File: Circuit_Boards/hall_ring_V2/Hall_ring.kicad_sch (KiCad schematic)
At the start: 18 parts, among them J1 T1M-06-X-DV, U1 DRV5053_LPG, U2 DRV5053_LPG, U3 DRV5053_LPG, U4 DRV5053_LPG, U5 DRV5053_LPG, U6 DRV5053_LPG, U7 DRV5053_LPG

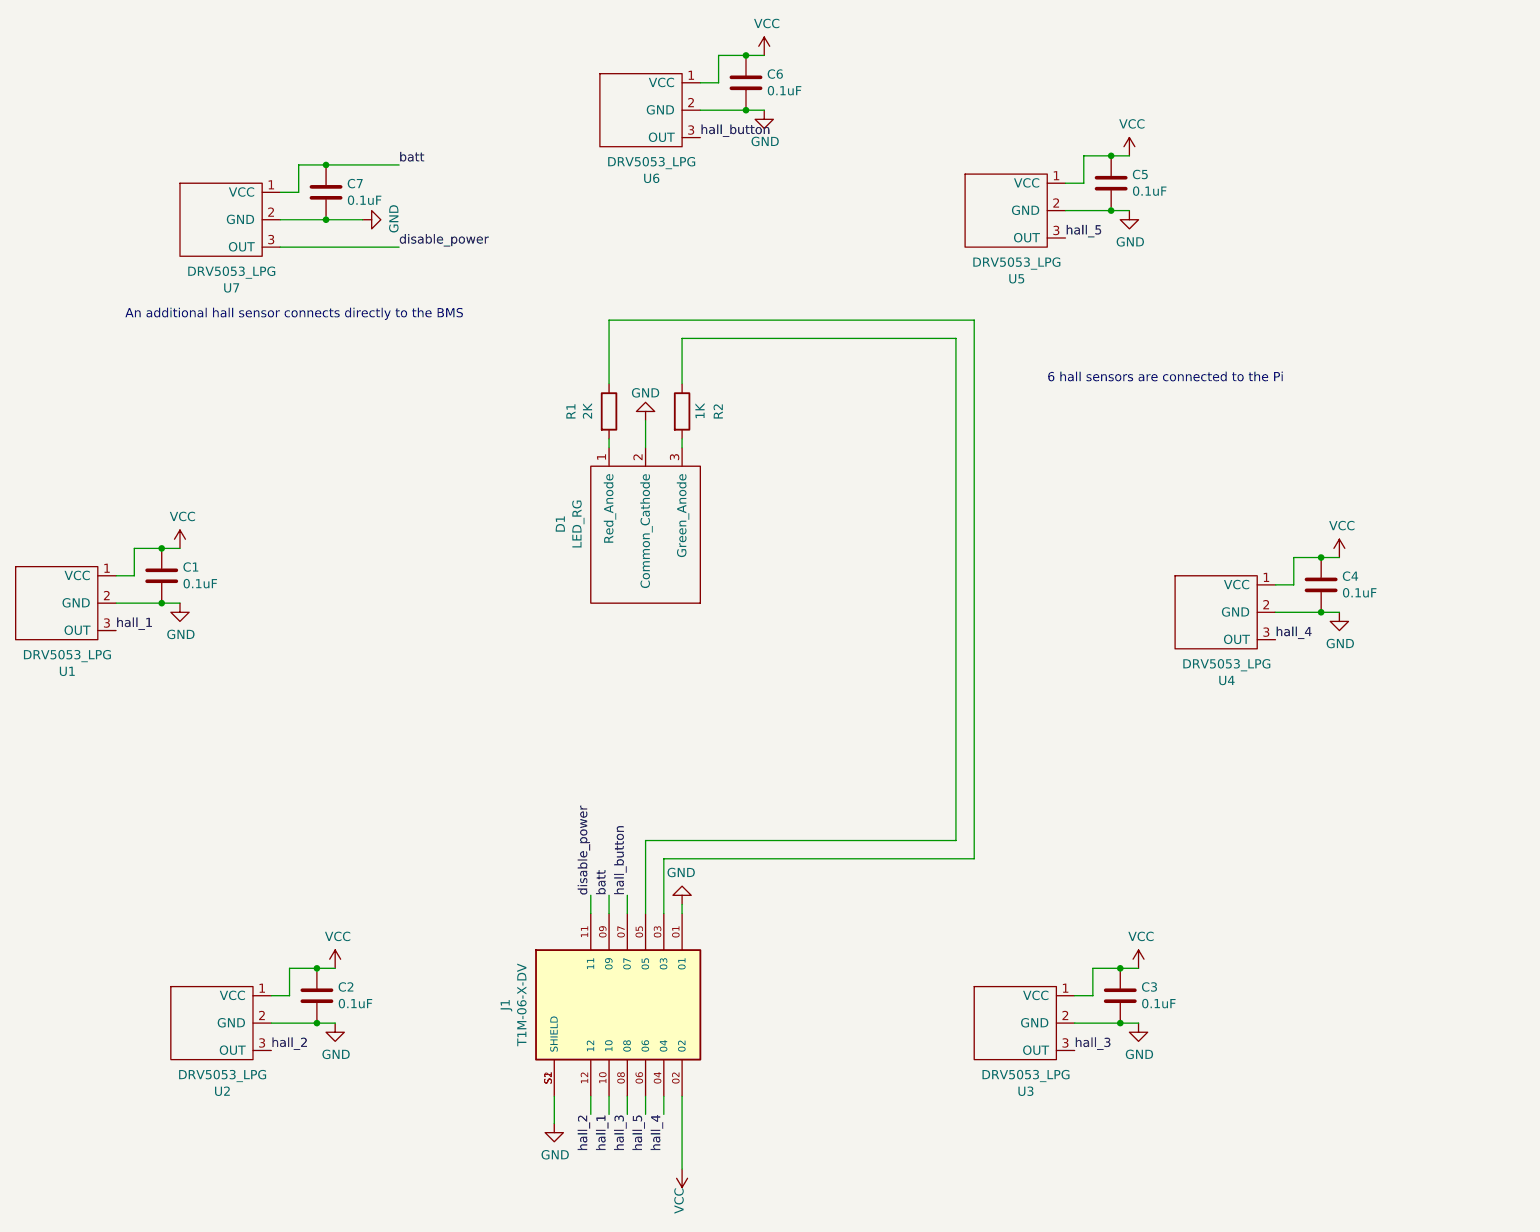
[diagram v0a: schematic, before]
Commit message: removed BOM and gerbers for kicad project, to ensure up to date exports
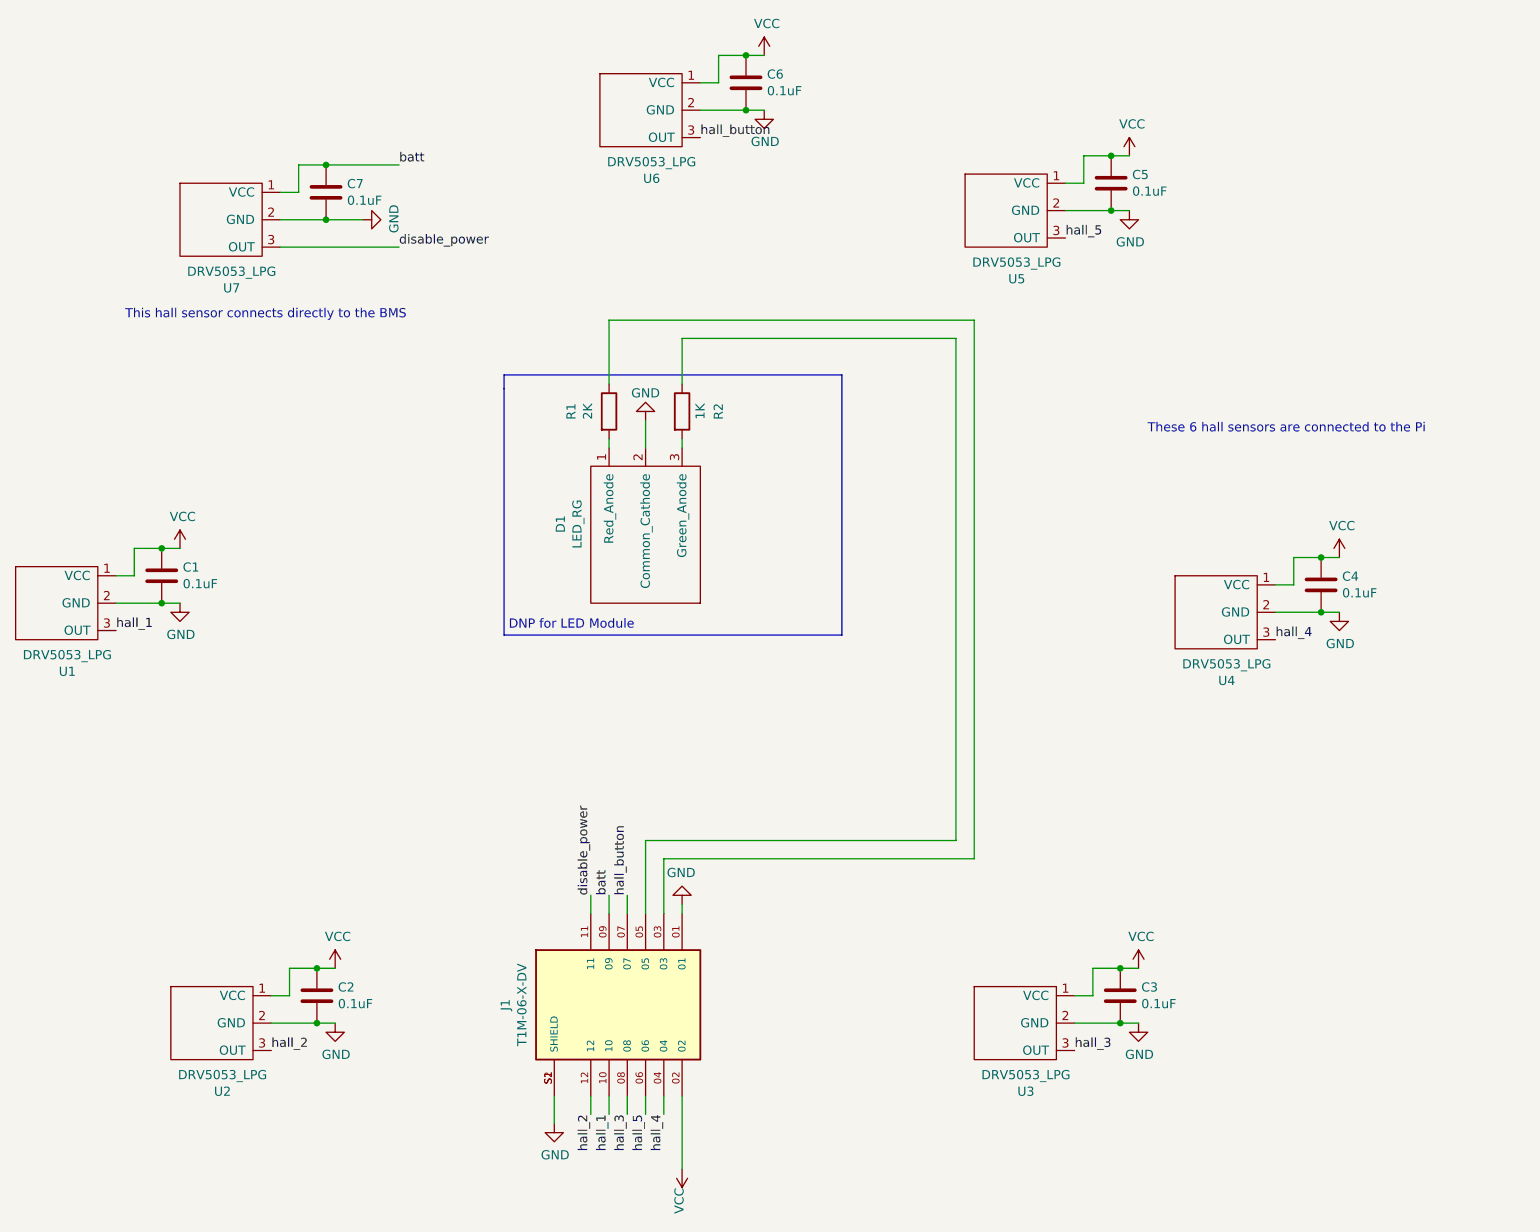
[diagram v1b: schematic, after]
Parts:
- C1, C2, C3, C4, C5, C6, C7, D1, J1, R1, R2, U1, U2, U3, U4, U5, U6, U7: Buy Digikey buy -> (none)
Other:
- note added: "DNP for LED Module"
- note added: "These 6 hall sensors are connected to the Pi"
- note added: "This hall sensor connects directly to the BMS"
- note removed: "6 hall sensors are connected to the Pi"
- note removed: "An additional hall sensor connects directly to the BMS"
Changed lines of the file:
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@@
+    (stroke (width 0) (type default) (color 0 0 0 0))
+  )
+  (polyline (pts (xy 165.735 63.5) (xy 118.745 63.5))
     (stroke (width 0) (type default) (color 0 0 0 0))
   )
@@
     (stroke (width 0) (type default) (color 0 0 0 0))
   )
+  (polyline (pts (xy 118.745 99.695) (xy 165.735 99.695))
+    (stroke (width 0) (type default) (color 0 0 0 0))
+  )
   (wire (pts (xy 92.71 146.05) (xy 95.25 146.05))
     (stroke (width 0) (type default) (color 0 0 0 0))
@@
     (stroke (width 0) (type default) (color 0 0 0 0))
   )
+  (polyline (pts (xy 118.745 65.405) (xy 118.745 99.695))
+    (stroke (width 0) (type default) (color 0 0 0 0))
+  )
   (wire (pts (xy 146.05 22.86) (xy 148.59 22.86))
     (stroke (width 0) (type default) (color 0 0 0 0))
@@
     (stroke (width 0) (type default) (color 0 0 0 0))
   )
+  (polyline (pts (xy 118.745 63.5) (xy 118.745 65.405))
+    (stroke (width 0) (type default) (color 0 0 0 0))
+  )
   (wire (pts (xy 181.61 128.27) (xy 181.61 58.42))
     (stroke (width 0) (type default) (color 0 0 0 0))
@@
     (stroke (width 0) (type default) (color 0 0 0 0))
   )
+  (polyline (pts (xy 165.735 99.695) (xy 165.735 63.5))
+    (stroke (width 0) (type default) (color 0 0 0 0))
+  )
   (wire (pts (xy 200.66 149.86) (xy 200.66 146.05))
     (stroke (width 0) (type default) (color 0 0 0 0))
@@
     (stroke (width 0) (type default) (color 0 0 0 0))
   )
-  (text "6 hall sensors are connected to the Pi\n" (at 194.31 64.77 0)
-    (effects (font (size 1.27 1.27)) (justify left bottom))
-  )
-  (text "An additional hall sensor connects directly to the BMS\n"
-    (at 66.04 55.88 0)
+  (text "DNP for LED Module" (at 119.38 99.06 0)
+    (effects (font (size 1.27 1.27)) (justify left bottom))
+  )
+  (text "These 6 hall sensors are connected to the Pi\n" (at 208.28 71.755 0)
+    (effects (font (size 1.27 1.27)) (justify left bottom))
+  )
+  (text "This hall sensor connects directly to the BMS\n" (at 66.04 55.88 0)
     (effects (font (size 1.27 1.27)) (justify left bottom))
   )
@@
       (effects (font (size 1.27 1.27)) hide)
     )
-    (property "Buy Digikey" "buy" (id 5) (at 57.15 101.6 0)
+    (property "Buy Digikey" "" (id 5) (at 57.15 101.6 0)
       (effects (font (size 1.27 1.27)) hide)
     )
@@
       (effects (font (size 1.27 1.27)) hide)
     )
-    (property "Buy Digikey" "buy" (id 5) (at 190.5 160.02 0)
+    (property "Buy Digikey" "" (id 5) (at 190.5 160.02 0)
       (effects (font (size 1.27 1.27)) hide)
     )
@@
       (effects (font (size 1.27 1.27)) hide)
     )
-    (property "Buy Digikey" "buy" (id 5) (at 218.44 102.87 0)
+    (property "Buy Digikey" "" (id 5) (at 218.44 102.87 0)
       (effects (font (size 1.27 1.27)) hide)
     )
@@
       (effects (font (size 1.27 1.27)) hide)
     )
-    (property "Buy Digikey" "buy" (id 5) (at 189.23 46.99 0)
+    (property "Buy Digikey" "" (id 5) (at 189.23 46.99 0)
       (effects (font (size 1.27 1.27)) hide)
     )
@@
       (effects (font (size 1.27 1.27)) hide)
     )
-    (property "Buy Digikey" "buy" (id 5) (at 138.43 33.02 0)
+    (property "Buy Digikey" "" (id 5) (at 138.43 33.02 0)
       (effects (font (size 1.27 1.27)) hide)
     )
@@
       (effects (font (size 1.27 1.27)) hide)
     )
-    (property "Buy Digikey" "buy" (id 5) (at 78.74 160.02 0)
+    (property "Buy Digikey" "" (id 5) (at 78.74 160.02 0)
       (effects (font (size 1.27 1.27)) hide)
     )
@@
       (effects (font (size 1.27 1.27)) hide)
     )
-    (property "Buy Digikey" "buy" (id 6) (at 71.12 91.44 0)
+    (property "Buy Digikey" "" (id 6) (at 71.12 91.44 0)
       (effects (font (size 1.27 1.27)) hide)
     )
@@
       (effects (font (size 1.27 1.27)) hide)
     )
-    (property "Buy Digikey" "buy" (id 6) (at 92.71 149.86 0)
+    (property "Buy Digikey" "" (id 6) (at 92.71 149.86 0)
       (effects (font (size 1.27 1.27)) hide)
     )
@@
       (effects (font (size 1.27 1.27)) hide)
     )
-    (property "Buy Digikey" "buy" (id 6) (at 204.47 149.86 0)
+    (property "Buy Digikey" "" (id 6) (at 204.47 149.86 0)
       (effects (font (size 1.27 1.27)) hide)
     )
@@
       (effects (font (size 1.27 1.27)) hide)
     )
-    (property "Buy Digikey" "buy" (id 6) (at 232.41 92.71 0)
+    (property "Buy Digikey" "" (id 6) (at 232.41 92.71 0)
       (effects (font (size 1.27 1.27)) hide)
     )
@@
       (effects (font (size 1.27 1.27)) hide)
     )
-    (property "Buy Digikey" "buy" (id 6) (at 203.2 36.83 0)
+    (property "Buy Digikey" "" (id 6) (at 203.2 36.83 0)
       (effects (font (size 1.27 1.27)) hide)
     )
@@
       (effects (font (size 1.27 1.27)) hide)
     )
-    (property "Buy Digikey" "buy" (id 6) (at 152.4 22.86 0)
+    (property "Buy Digikey" "" (id 6) (at 152.4 22.86 0)
       (effects (font (size 1.27 1.27)) hide)
     )
@@
       (effects (font (size 1.27 1.27)) hide)
     )
-    (property "Buy Digikey" "buy" (id 5) (at 80.01 48.26 0)
+    (property "Buy Digikey" "" (id 5) (at 80.01 48.26 0)
       (effects (font (size 1.27 1.27)) hide)
     )
@@
       (effects (font (size 1.27 1.27)) hide)
     )
-    (property "Buy Digikey" "buy" (id 6) (at 93.98 38.1 0)
+    (property "Buy Digikey" "" (id 6) (at 93.98 38.1 0)
       (effects (font (size 1.27 1.27)) hide)
     )
@@
       (effects (font (size 1.27 1.27)) hide)
     )
-    (property "Buy Digikey" "buy" (id 5) (at 130.81 83.82 0)
+    (property "Buy Digikey" "" (id 5) (at 130.81 83.82 0)
       (effects (font (size 1.27 1.27)) hide)
     )
@@
       (effects (font (size 1.27 1.27)) hide)
     )
-    (property "Buy Digikey" "buy" (id 6) (at 133.35 68.58 0)
+    (property "Buy Digikey" "" (id 6) (at 133.35 68.58 0)
       (effects (font (size 1.27 1.27)) hide)
     )
@@
       (effects (font (size 1.27 1.27)) hide)
     )
-    (property "Buy Digikey" "buy" (id 6) (at 143.51 68.58 0)
+    (property "Buy Digikey" "" (id 6) (at 143.51 68.58 0)
       (effects (font (size 1.27 1.27)) hide)
     )
@@
       (effects (font (size 1.27 1.27)) hide)
     )
-    (property "Buy Digikey" "buy" (id 9) (at 135.89 151.13 0)
-      (effects (font (size 1.27 1.27)) hide)
-    )
+    (property "Buy Digikey" "" (id 9) (at 135.89 151.13 0)
+      (effects (font (size 1.27 1.27)) hide)
+    )
